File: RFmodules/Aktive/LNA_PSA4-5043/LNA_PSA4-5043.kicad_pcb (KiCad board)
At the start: 2 copper layers, 32 x 18 mm, 15 parts, among them J1 SMA, J2 SMA, U1 PSA4-5043+

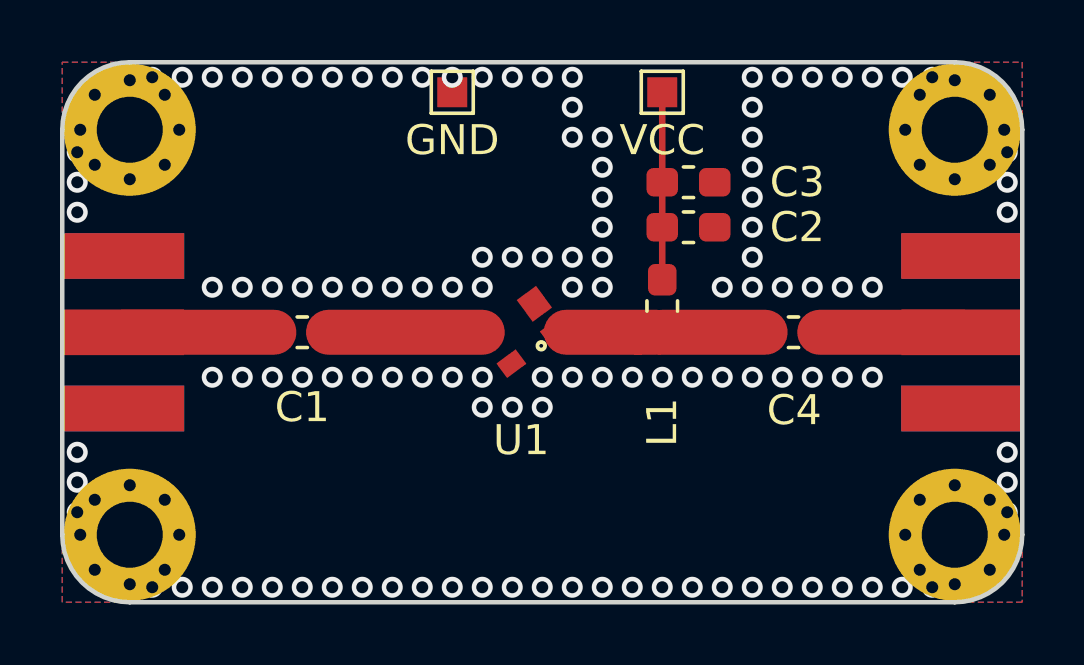
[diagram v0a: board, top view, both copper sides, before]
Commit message: Add power LED and fix SMA clearance
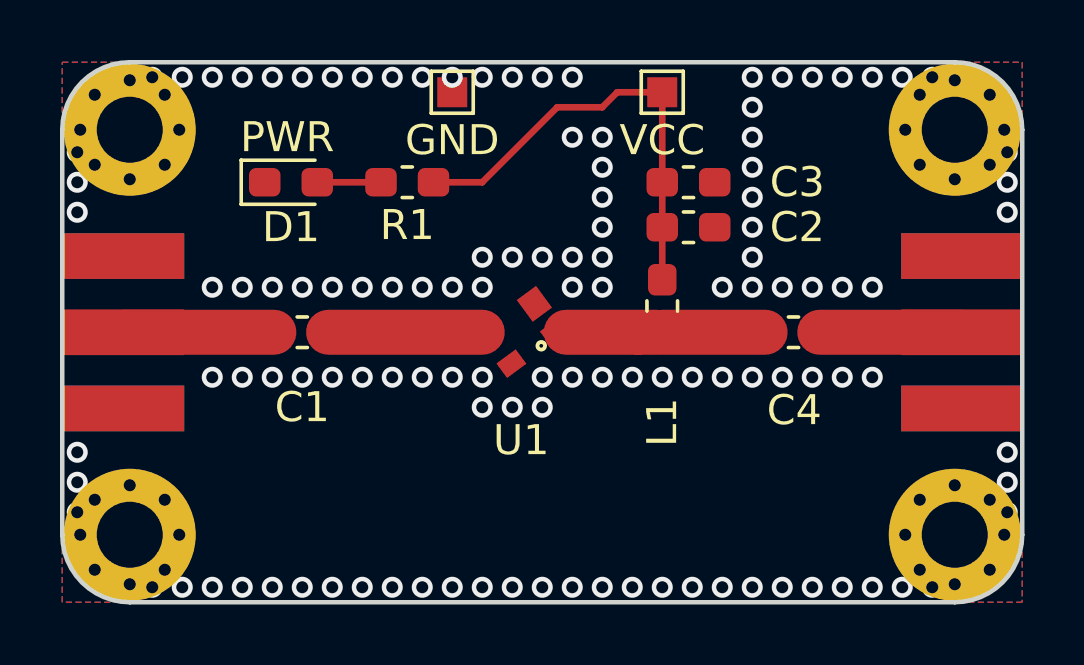
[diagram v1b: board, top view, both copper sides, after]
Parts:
- added D1: LED, LED_SMD:LED_0603_1608Metric_Pad1.05x0.95mm_HandSolder, F.Cu at (107.6, 104.0)
- added R1: R, Resistor_SMD:R_0603_1608Metric_Pad1.05x0.95mm_HandSolder, F.Cu at (111.5, 104.0)
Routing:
- net Net-(C2-Pad2): track 6.25 -> 15.1 mm
- net Net-(D1-Pad2): track 0.00 -> 2.12 mm
- net GND: vias 121 -> 120
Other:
- board text added: "LNA - PSA4-5043+ Revision 3 - 03/2019 github.com/fgaletsee/RFLego"
- board text added: "PWR"
- board text removed: "LNA - PSA4-5043+ Revision 2 - 02/2019 github.com/fgaletsee/RFLego"
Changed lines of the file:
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@@
   (general
     (thickness 1.6)
-    (drawings 27)
-    (tracks 130)
+    (drawings 30)
+    (tracks 135)
     (zones 0)
-    (modules 15)
-    (nets 7)
+    (modules 17)
+    (nets 8)
   )
   (page A4)
@@
     (47 F.CrtYd user)
     (48 B.Fab user)
-    (49 F.Fab user)
+    (49 F.Fab user hide)
   )
   (setup
@@
   (net 5 "Net-(C4-Pad2)")
   (net 6 "Net-(C4-Pad1)")
+  (net 7 "Net-(D1-Pad2)")
   (net_class Default "This is the default net class."
     (clearance 0.2)
@@
     (add_net GND)
     (add_net "Net-(C2-Pad2)")
+    (add_net "Net-(D1-Pad2)")
   )
   (net_class "50 Ohm thin" ""
@@
       (xy -3.43224 -2.584467) (xy -3.324904 -2.572722) (xy -3.231114 -2.584505)) (layer B.SilkS) (width 0.01))
   )
+  (module LED_SMD:LED_0603_1608Metric_Pad1.05x0.95mm_HandSolder (layer F.Cu)
+    (at 107.625 104)
+    (descr "LED SMD 0603 (1608 Metric), square (rectangular) end terminal, IPC_7351 nominal, (Body size source: http://www.tortai-tech.com/upload/download/2011102023233369053.pdf), generated with kicad-footprint-generator")
+    (tags "LED handsolder")
+    (attr smd)
+    (fp_text reference D1 (at 0 1.5) (layer F.SilkS)
+      (effects (font (size 1 1) (thickness 0.15)))
+    )
+    (fp_text value LED (at 0 1.43) (layer F.Fab)
+      (effects (font (size 1 1) (thickness 0.15)))
+    )
+    (fp_line (start 0.8 -0.4) (end -0.5 -0.4) (layer F.Fab) (width 0.1))
+    (fp_line (start -0.5 -0.4) (end -0.8 -0.1) (layer F.Fab) (width 0.1))
+    (fp_line (start -0.8 -0.1) (end -0.8 0.4) (layer F.Fab) (width 0.1))
+    (fp_line (start -0.8 0.4) (end 0.8 0.4) (layer F.Fab) (width 0.1))
+    (fp_line (start 0.8 0.4) (end 0.8 -0.4) (layer F.Fab) (width 0.1))
+    (fp_line (start 0.8 -0.735) (end -1.66 -0.735) (layer F.SilkS) (width 0.12))
+    (fp_line (start -1.66 -0.735) (end -1.66 0.735) (layer F.SilkS) (width 0.12))
+    (fp_line (start -1.66 0.735) (end 0.8 0.735) (layer F.SilkS) (width 0.12))
+    (fp_line (start -1.65 0.73) (end -1.65 -0.73) (layer F.CrtYd) (width 0.05))
+    (fp_line (start -1.65 -0.73) (end 1.65 -0.73) (layer F.CrtYd) (width 0.05))
+    (fp_line (start 1.65 -0.73) (end 1.65 0.73) (layer F.CrtYd) (width 0.05))
+    (fp_line (start 1.65 0.73) (end -1.65 0.73) (layer F.CrtYd) (width 0.05))
+    (fp_text user %R (at 0 0) (layer F.Fab)
+      (effects (font (size 0.4 0.4) (thickness 0.06)))
+    )
+    (pad 1 smd roundrect (at -0.875 0) (size 1.05 0.95) (layers F.Cu F.Paste F.Mask) (roundrect_rratio 0.25)
+      (net 1 GND))
+    (pad 2 smd roundrect (at 0.875 0) (size 1.05 0.95) (layers F.Cu F.Paste F.Mask) (roundrect_rratio 0.25)
+      (net 7 "Net-(D1-Pad2)"))
+    (model ${KISYS3DMOD}/LED_SMD.3dshapes/LED_0603_1608Metric.wrl
+      (at (xyz 0 0 0))
+      (scale (xyz 1 1 1))
+      (rotate (xyz 0 0 0))
+    )
+  )
+  (module Resistor_SMD:R_0603_1608Metric_Pad1.05x0.95mm_HandSolder (layer F.Cu)
+    (at 111.5 104 180)
+    (descr "Resistor SMD 0603 (1608 Metric), square (rectangular) end terminal, IPC_7351 nominal with elongated pad for handsoldering. (Body size source: http://www.tortai-tech.com/upload/download/2011102023233369053.pdf), generated with kicad-footprint-generator")
+    (tags "resistor handsolder")
+    (attr smd)
+    (fp_text reference R1 (at 0 -1.43 180) (layer F.SilkS)
+      (effects (font (size 1 1) (thickness 0.15)))
+    )
+    (fp_text value R (at 0 1.43 180) (layer F.Fab)
+      (effects (font (size 1 1) (thickness 0.15)))
+    )
+    (fp_line (start -0.8 0.4) (end -0.8 -0.4) (layer F.Fab) (width 0.1))
+    (fp_line (start -0.8 -0.4) (end 0.8 -0.4) (layer F.Fab) (width 0.1))
+    (fp_line (start 0.8 -0.4) (end 0.8 0.4) (layer F.Fab) (width 0.1))
+    (fp_line (start 0.8 0.4) (end -0.8 0.4) (layer F.Fab) (width 0.1))
+    (fp_line (start -0.171267 -0.51) (end 0.171267 -0.51) (layer F.SilkS) (width 0.12))
+    (fp_line (start -0.171267 0.51) (end 0.171267 0.51) (layer F.SilkS) (width 0.12))
+    (fp_line (start -1.65 0.73) (end -1.65 -0.73) (layer F.CrtYd) (width 0.05))
+    (fp_line (start -1.65 -0.73) (end 1.65 -0.73) (layer F.CrtYd) (width 0.05))
+    (fp_line (start 1.65 -0.73) (end 1.65 0.73) (layer F.CrtYd) (width 0.05))
+    (fp_line (start 1.65 0.73) (end -1.65 0.73) (layer F.CrtYd) (width 0.05))
+    (fp_text user %R (at 0 0 180) (layer F.Fab)
+      (effects (font (size 0.4 0.4) (thickness 0.06)))
+    )
+    (pad 1 smd roundrect (at -0.875 0 180) (size 1.05 0.95) (layers F.Cu F.Paste F.Mask) (roundrect_rratio 0.25)
+      (net 4 "Net-(C2-Pad2)"))
+    (pad 2 smd roundrect (at 0.875 0 180) (size 1.05 0.95) (layers F.Cu F.Paste F.Mask) (roundrect_rratio 0.25)
+      (net 7 "Net-(D1-Pad2)"))
+    (model ${KISYS3DMOD}/Resistor_SMD.3dshapes/R_0603_1608Metric.wrl
+      (at (xyz 0 0 0))
+      (scale (xyz 1 1 1))
+      (rotate (xyz 0 0 0))
+    )
+  )
+  (gr_text PWR (at 107.5 102.5) (layer F.SilkS)
+    (effects (font (size 1 1) (thickness 0.15)))
+  )
+  (gr_line (start 132 102.25) (end 132 106.27) (layer F.Mask) (width 2))
+  (gr_line (start 100 102.25) (end 100 106.27) (layer F.Mask) (width 2))
   (gr_line (start 102.25 100) (end 117 100) (layer B.Mask) (width 2))
   (gr_line (start 123 100) (end 129.75 100) (layer B.Mask) (width 2))
   (gr_line (start 123 100) (end 129.75 100) (layer F.Mask) (width 2))
-  (gr_text "LNA - PSA4-5043+\nRevision 2 - 02/2019\ngithub.com/fgaletsee/RFLego" (at 127.75 106.25) (layer B.SilkS)
+  (gr_text "LNA - PSA4-5043+\nRevision 3 - 03/2019\ngithub.com/fgaletsee/RFLego" (at 127.75 106.25) (layer B.SilkS)
     (effects (font (size 1 1) (thickness 0.25)) (justify left mirror))
   )
@@
   (gr_line (start 132 102.25) (end 132 115.75) (layer Edge.Cuts) (width 0.15))
   (gr_line (start 100 102.25) (end 100 115.75) (layer B.Mask) (width 2))
-  (gr_line (start 100 102.25) (end 100 115.75) (layer F.Mask) (width 2))
+  (gr_line (start 100 111.73) (end 100 115.75) (layer F.Mask) (width 2))
   (gr_line (start 102.25 118) (end 129.75 118) (layer B.Mask) (width 2))
   (gr_line (start 102.25 118) (end 129.75 118) (layer F.Mask) (width 2))
@@
   (gr_arc (start 102.25 102.25) (end 102.25 100) (angle -90) (layer Edge.Cuts) (width 0.15))
   (gr_arc (start 102.25 115.75) (end 100 115.75) (angle -90) (layer B.Mask) (width 2))
-  (gr_line (start 132 102.25) (end 132 115.75) (layer F.Mask) (width 2))
+  (gr_line (start 132 111.73) (end 132 115.75) (layer F.Mask) (width 2))
   (gr_line (start 102.25 118) (end 129.75 118) (layer Edge.Cuts) (width 0.15))
   (gr_line (start 100 102.25) (end 100 115.75) (layer Edge.Cuts) (width 0.15))
   (gr_line (start 102.25 100) (end 117 100) (layer F.Mask) (width 2))
+  (via (at 118 103.5) (size 0.7) (drill 0.4) (layers F.Cu B.Cu) (net 1))
+  (via (at 118 104.5) (size 0.7) (drill 0.4) (layers F.Cu B.Cu) (net 1))
   (via (at 127 110.5) (size 0.7) (drill 0.4) (layers F.Cu B.Cu) (net 1))
   (via (at 126 110.5) (size 0.7) (drill 0.4) (layers F.Cu B.Cu) (net 1))
@@
   (via (at 123 102.5) (size 0.7) (drill 0.4) (layers F.Cu B.Cu) (net 1))
   (via (at 123 101.5) (size 0.7) (drill 0.4) (layers F.Cu B.Cu) (net 1))
-  (via (at 117 101.5) (size 0.7) (drill 0.4) (layers F.Cu B.Cu) (net 1))
   (via (at 117 102.5) (size 0.7) (drill 0.4) (layers F.Cu B.Cu) (net 1))
   (via (at 118 102.5) (size 0.7) (drill 0.4) (layers F.Cu B.Cu) (net 1))
-  (via (at 118 103.5) (size 0.7) (drill 0.4) (layers F.Cu B.Cu) (net 1))
-  (via (at 118 104.5) (size 0.7) (drill 0.4) (layers F.Cu B.Cu) (net 1))
   (via (at 118 105.5) (size 0.7) (drill 0.4) (layers F.Cu B.Cu) (net 1))
   (via (at 118 106.5) (size 0.7) (drill 0.4) (layers F.Cu B.Cu) (net 1))
@@
   (segment (start 120 105.5) (end 120 104) (width 0.22) (layer F.Cu) (net 4))
   (segment (start 120 104) (end 120 101) (width 0.22) (layer F.Cu) (net 4))
+  (segment (start 120 101) (end 118.5 101) (width 0.22) (layer F.Cu) (net 4))
+  (segment (start 118.5 101) (end 118 101.5) (width 0.22) (layer F.Cu) (net 4))
+  (segment (start 118 101.5) (end 116.5 101.5) (width 0.22) (layer F.Cu) (net 4))
+  (segment (start 114 104) (end 112.375 104) (width 0.22) (layer F.Cu) (net 4))
+  (segment (start 116.5 101.5) (end 114 104) (width 0.22) (layer F.Cu) (net 4))
   (segment (start 119.163924 109) (end 116.8 109) (width 1.5) (layer F.Cu) (net 5))
   (segment (start 120 109) (end 123.42999 109) (width 1.5) (layer F.Cu) (net 5))
   (segment (start 119.8 109) (end 119.225 109) (width 1.5) (layer F.Cu) (net 5))
   (segment (start 130 109) (end 125.25 109) (width 1.5) (layer F.Cu) (net 6))
+  (segment (start 110.625 104) (end 108.5 104) (width 0.22) (layer F.Cu) (net 7))
   (zone (net 1) (net_name GND) (layer F.Cu) (hatch edge 0.508)
     (connect_pads yes (clearance 0))
